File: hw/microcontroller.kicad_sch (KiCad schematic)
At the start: 66 parts, among them J201 68710814022, J202 FTSH-105-01-L-DV-K, SW201 Push button switch, U201 STM32H753VITx, U202 USB3343, Y201 26MHz, Y202 26MHz

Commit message: Starting some layout
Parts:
- removed C210, C211: 100nF, Capacitor_SMD:C_0402_1005Metric, symbol Device:C
- removed C212: 4.7uF, Capacitor_SMD:C_0805_2012Metric, symbol Device:C
- removed FB201: 600, Inductor_SMD:L_0603_1608Metric, symbol Device:FerriteBead_Small
- SW501: renamed from SW201; footprint Library:Panasonic_EVQPUK_EVQPUB -> Library:EVQPUC02K
- renumbered C201 to C501, C202 to C502, C203 to C503, C204 to C504, C205 to C505, C206 to C506, C207 to C507, C208 to C508, C209 to C509, C213 to C510, C214 to C511, C217 to C512, C218 to C513, C219 to C514, C220 to C515, C221 to C516, C222 to C517, C223 to C518, C224 to C519, C225 to C520, C226 to C521, C227 to C522, C228 to C523, C229 to C524, C215 to C525, C216 to C526, C230 to C527, C231 to C528, D201 to D501, J201 to J501, J202 to J502, PG201 to PG501, R201 to R501, R202 to R502, R204 to R503, R501 to R504, R206 to R505, R207 to R506, R208 to R507, R220 to R508, R210 to R509, R218 to R510, R211 to R511, R212 to R512, R214 to R513, R209 to R514, R216 to R515, R205 to R516, R217 to R517, R219 to R518, R221 to R519, R226 to R520, R227 to R521, R222 to R522, R223 to R523, R228 to R524, R502 to R525, U201 to U501, U202 to U502, Y201 to Y501, Y202 to Y502
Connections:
- net +3.3V-ON is gone; now on net +3.3V: C501.2, C516.1, C517.1, C518.1, C519.1, C520.1, C521.1, C522.1, C523.1, C524.1, J502.1 (VTref), R501.1, R521.1, U501.100 (VDD), U501.11 (VDD), U501.27 (VDD), U501.50 (VDD), U501.6 (VBAT), U501.75 (VDD)
- net enable3V3 is gone; now on net enable5VA: U501.87 (PD6)
- net enable5VA: no longer U501.55 (PD8)
- net +MC3VA renamed +3.3VA
- no-connect marks 35 -> 36
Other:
- moved on the sheet: C525, C526, R522

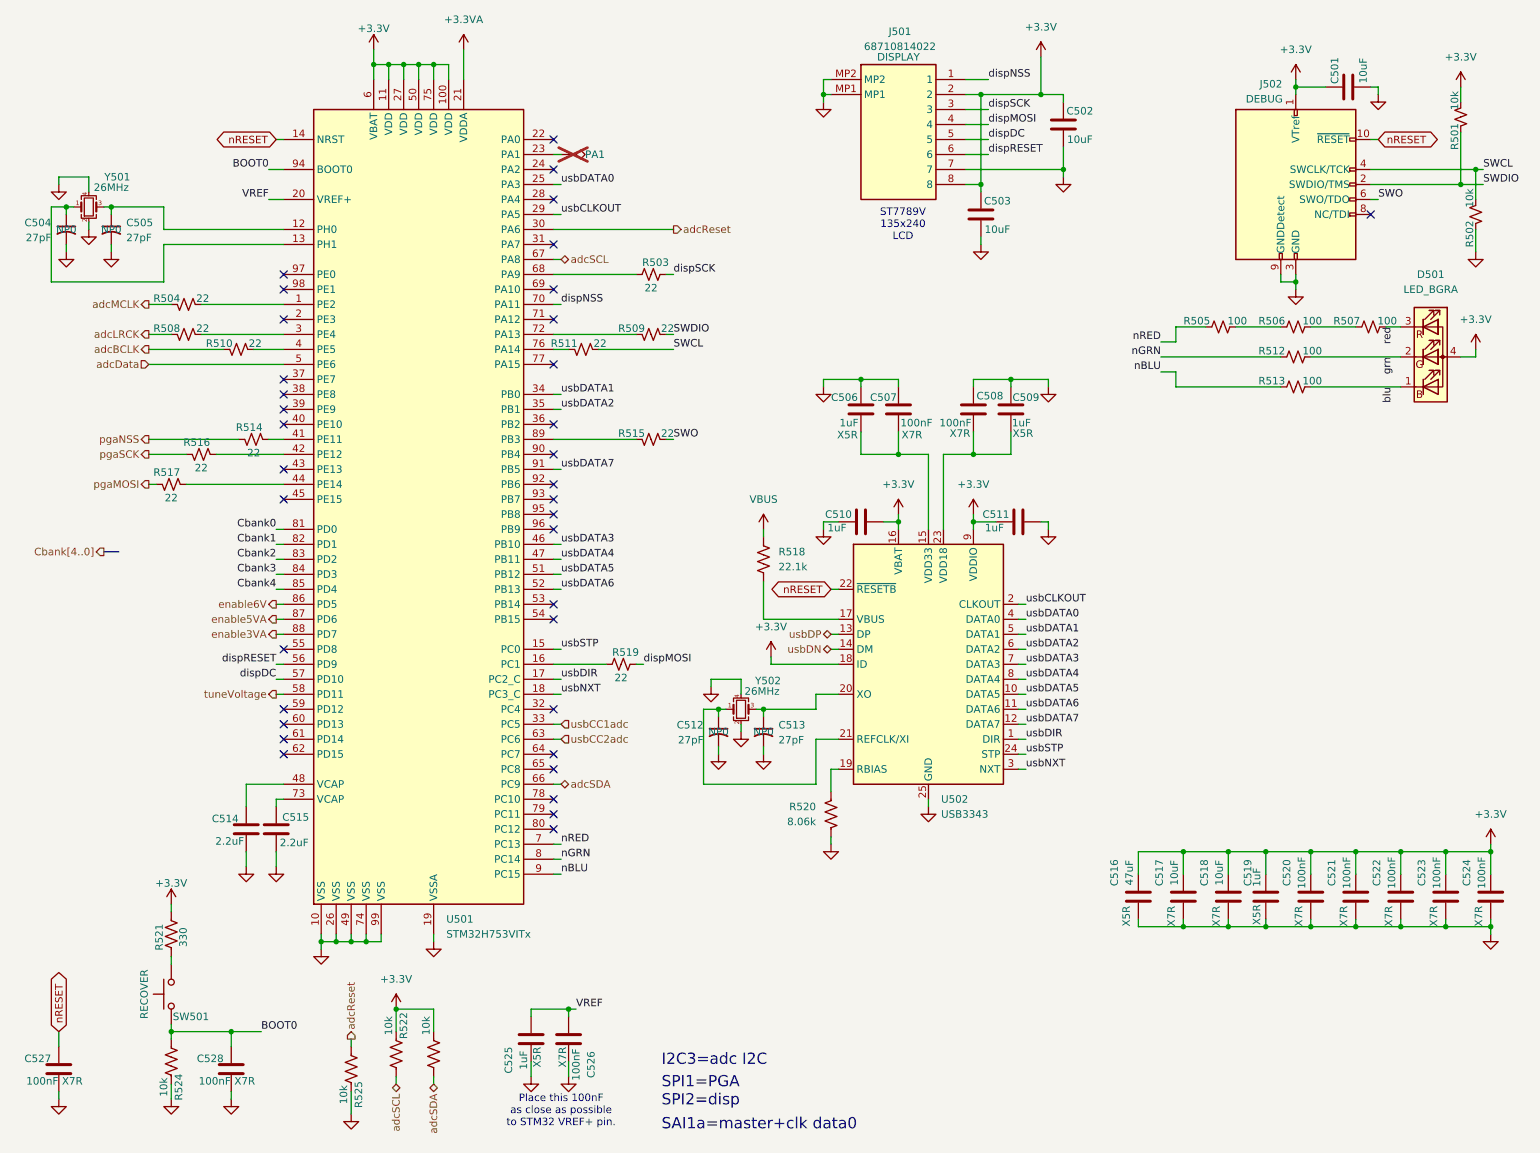
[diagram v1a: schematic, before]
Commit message: Routing complete for DVT1 all ERC and DRC pass, 3D view is full
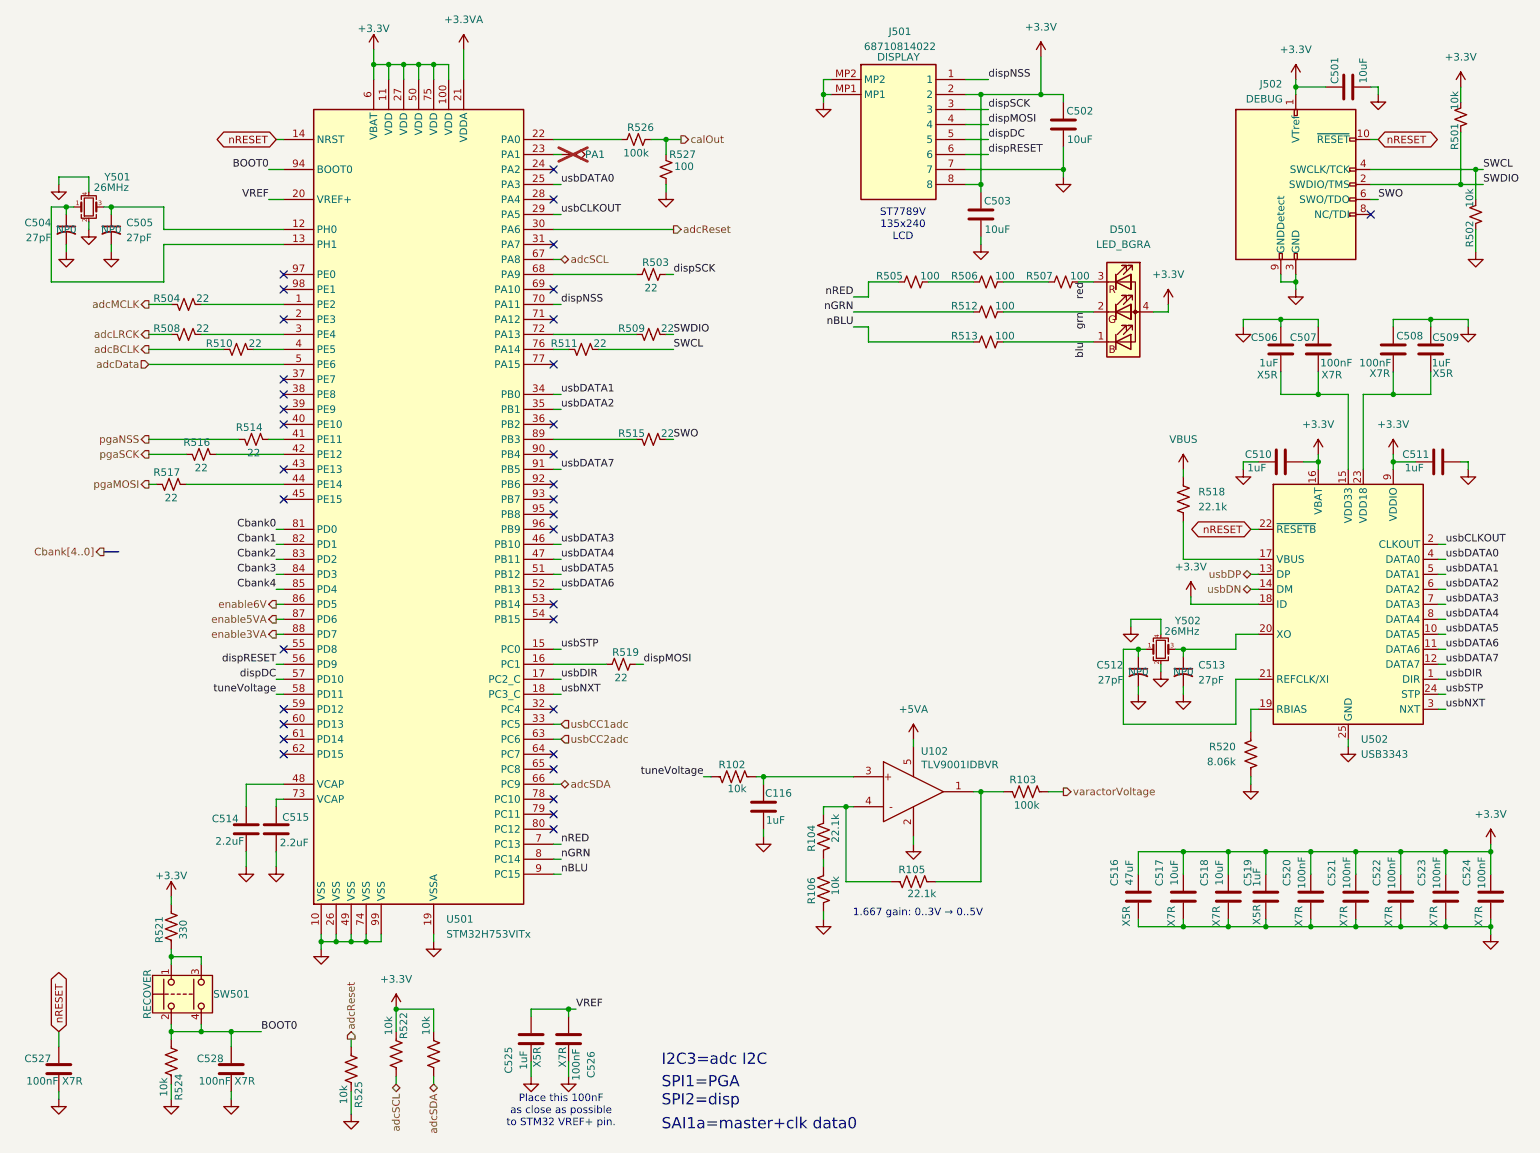
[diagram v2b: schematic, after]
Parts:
- added C116: 1uF, Capacitor_SMD:C_0402_1005Metric, symbol Device:C
- added R102, R106: 10k, Resistor_SMD:R_0402_1005Metric, symbol Device:R_US
- added R103: 100k, Resistor_SMD:R_0402_1005Metric, symbol Device:R_US
- added R104, R105: 22.1k, Resistor_SMD:R_0402_1005Metric, symbol Device:R_US
- added R526: 100k, Resistor_SMD:R_0402_1005Metric, symbol Device:R_Small_US
- added R527: 100, Resistor_SMD:R_0402_1005Metric, symbol Device:R_Small_US
- added U102: TLV9001IDBVR, Library:SOT95P280X145-5N, symbol Library:TLV9001IDBVR
- R520: footprint Resistor_SMD:R_0603_1608Metric -> Resistor_SMD:R_0402_1005Metric
- SW501: symbol Switch:SW_Push -> Switch:SW_Push_Dual
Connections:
- net BOOT0: now also SW501.4
- net GND: now also C116.1, R106.2, R527.1, U102.2 (V-)
- net tuneVoltage: now also R102.2
- net at R521.2, SW501.1: now also SW501.3
- net at U501.22 (PA0): now also R526.1
- new net: R104.2, R106.1
- new net: R103.2, R105.1, U102.1 (OUT)
- new net: C116.2, R102.1, U102.3 (IN+)
- new net: R104.1, R105.2, U102.4 (IN-)
- new net +5VA: U102.5 (V+)
- new net calOut: R526.2, R527.2
- new net varactorVoltage: R103.1
- no-connect marks 36 -> 35
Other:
- note added: "1.667 gain: 0..3V → 0..5V"
- moved on the sheet: C506, C507, C508, C509, C510, C511, C512, C513, D501, R505, R506, R507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
